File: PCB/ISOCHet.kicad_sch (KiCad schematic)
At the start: 19 parts, among them J1 USB_C_Receptacle_USB2.0, J2 Conn_01x08_Pin, SW0 BOOT, SW1 TAB, SW2 ENTER, SW3 CAPS, SW4 CAPS_STEP1.5, SW5 CAPS_STEP1.25, U1 CH552G, U2 USBLC6-2P6

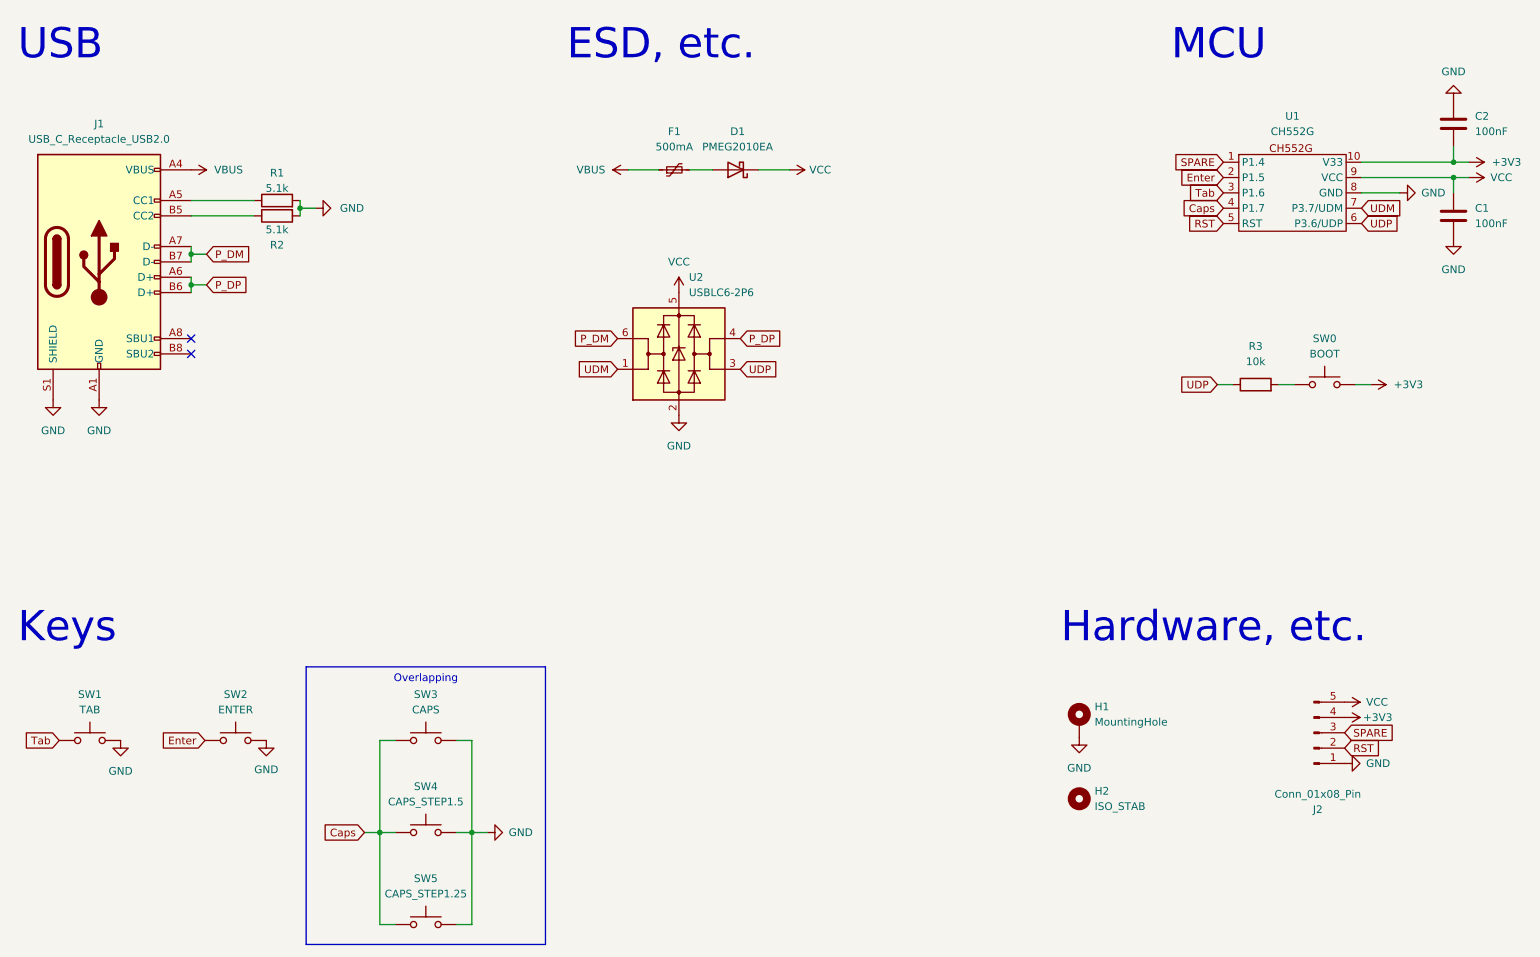
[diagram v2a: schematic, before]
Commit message: Move all components to front
USB data pins on port now line up with CH552E and do not need to crossover.
R1 and R2 remain on back.
Tweaked overlapping Caps Lock switch footprints to reduce DRC errors.
Power tracks are now 0.3mm to match maximum width of CH552E pads.
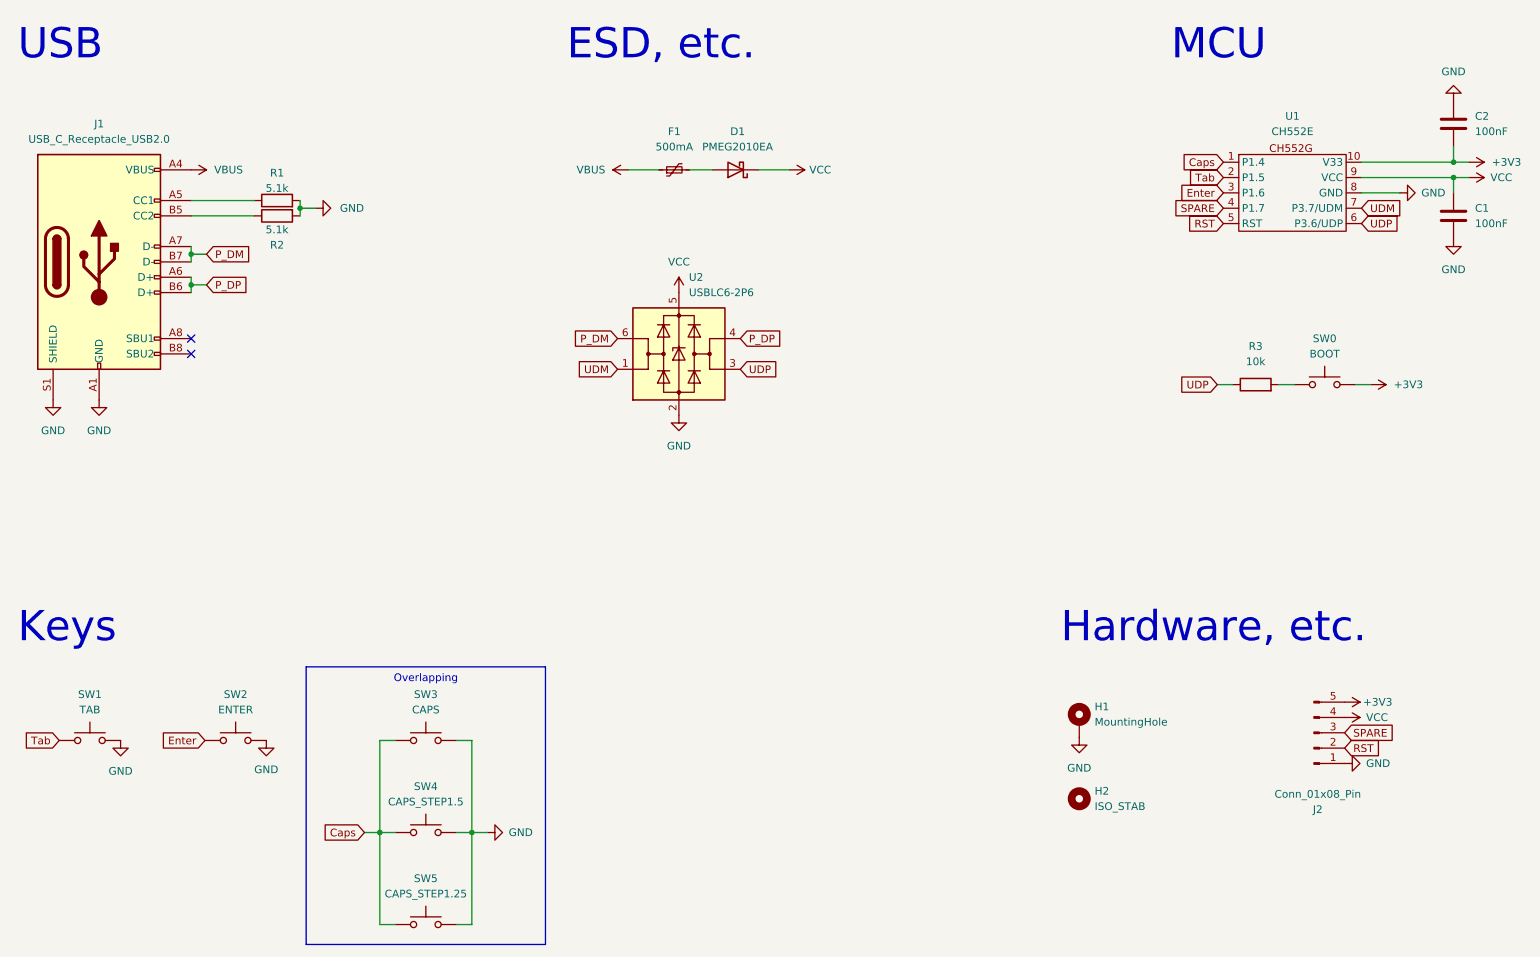
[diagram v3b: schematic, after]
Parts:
- U1: value CH552G -> CH552E; LCSC C111292 -> C967938
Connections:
- net +3V3: now also J2.5 (Pin_5); no longer J2.4 (Pin_4)
- net Caps: now also SW3.1, SW4.1, SW5.1, U1.1 (P1.4); no longer SW3.2, SW4.2, SW5.2, U1.4 (P1.7)
- net Enter: now also U1.3 (P1.6); no longer U1.2 (P1.5)
- net GND: now also SW1.2, SW3.2, SW4.2, SW5.2; no longer SW1.1, SW3.1, SW4.1, SW5.1
- net SPARE: now also U1.4 (P1.7); no longer U1.1 (P1.4)
- net Tab: now also SW1.1, U1.2 (P1.5); no longer SW1.2, U1.3 (P1.6)
- net VCC: now also J2.4 (Pin_4); no longer J2.5 (Pin_5)
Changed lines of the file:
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@@
     )
   )
-  (global_label "Caps" (shape input) (at 217.424 46.99 180) (fields_autoplaced)
+  (global_label "Caps" (shape input) (at 217.424 39.37 180) (fields_autoplaced)
     (effects (font (size 1.27 1.27)) (justify right))
-    (property "Intersheetrefs" "${INTERSHEET_REFS}" (at 209.8427 46.99 0)
+    (property "Intersheetrefs" "${INTERSHEET_REFS}" (at 209.8427 39.37 0)
       (effects (font (size 1.27 1.27)) (justify right) hide)
     )
@@
     )
   )
-  (global_label "Tab" (shape input) (at 217.424 44.45 180) (fields_autoplaced)
+  (global_label "Tab" (shape input) (at 217.424 41.91 180) (fields_autoplaced)
     (effects (font (size 1.27 1.27)) (justify right))
-    (property "Intersheetrefs" "${INTERSHEET_REFS}" (at 211.1732 44.45 0)
+    (property "Intersheetrefs" "${INTERSHEET_REFS}" (at 211.1732 41.91 0)
       (effects (font (size 1.27 1.27)) (justify right) hide)
     )
@@
     )
   )
-  (global_label "Enter" (shape input) (at 217.424 41.91 180) (fields_autoplaced)
+  (global_label "Enter" (shape input) (at 217.424 44.45 180) (fields_autoplaced)
     (effects (font (size 1.27 1.27)) (justify right))
-    (property "Intersheetrefs" "${INTERSHEET_REFS}" (at 209.5403 41.91 0)
+    (property "Intersheetrefs" "${INTERSHEET_REFS}" (at 209.5403 44.45 0)
       (effects (font (size 1.27 1.27)) (justify right) hide)
     )
   )
-  (global_label "SPARE" (shape input) (at 217.424 39.37 180) (fields_autoplaced)
+  (global_label "SPARE" (shape input) (at 217.424 46.99 180) (fields_autoplaced)
     (effects (font (size 1.27 1.27)) (justify right))
-    (property "Intersheetrefs" "${INTERSHEET_REFS}" (at 208.4517 39.37 0)
+    (property "Intersheetrefs" "${INTERSHEET_REFS}" (at 208.4517 46.99 0)
       (effects (font (size 1.27 1.27)) (justify right) hide)
     )
@@
     )
   )
-  (symbol (lib_id "power:+3V3") (at 237.49 131.318 270) (unit 1)
+  (symbol (lib_id "power:+3V3") (at 237.49 128.778 270) (unit 1)
     (in_bom yes) (on_board yes) (dnp no)
-    (property "Reference" "#PWR020" (at 233.68 131.318 0)
-      (effects (font (size 1.27 1.27)) hide)
-    )
-    (property "Value" "+3V3" (at 240.538 131.318 90)
-      (effects (font (size 1.27 1.27)) (justify left))
-    )
-    (property "Footprint" "" (at 237.49 131.318 0)
-      (effects (font (size 1.27 1.27)) hide)
-    )
-    (property "Datasheet" "" (at 237.49 131.318 0)
+    (property "Reference" "#PWR020" (at 233.68 128.778 0)
+      (effects (font (size 1.27 1.27)) hide)
+    )
+    (property "Value" "+3V3" (at 240.538 128.778 90)
+      (effects (font (size 1.27 1.27)) (justify left))
+    )
+    (property "Footprint" "" (at 237.49 128.778 0)
+      (effects (font (size 1.27 1.27)) hide)
+    )
+    (property "Datasheet" "" (at 237.49 128.778 0)
       (effects (font (size 1.27 1.27)) hide)
     )
@@
     )
   )
-  (symbol (lib_id "power:VCC") (at 237.49 128.778 270) (unit 1)
+  (symbol (lib_id "power:VCC") (at 237.49 131.318 270) (unit 1)
     (in_bom yes) (on_board yes) (dnp no)
-    (property "Reference" "#PWR022" (at 233.68 128.778 0)
-      (effects (font (size 1.27 1.27)) hide)
-    )
-    (property "Value" "VCC" (at 241.046 128.778 90)
-      (effects (font (size 1.27 1.27)) (justify left))
-    )
-    (property "Footprint" "" (at 237.49 128.778 0)
-      (effects (font (size 1.27 1.27)) hide)
-    )
-    (property "Datasheet" "" (at 237.49 128.778 0)
+    (property "Reference" "#PWR022" (at 233.68 131.318 0)
+      (effects (font (size 1.27 1.27)) hide)
+    )
+    (property "Value" "VCC" (at 241.046 131.318 90)
+      (effects (font (size 1.27 1.27)) (justify left))
+    )
+    (property "Footprint" "" (at 237.49 131.318 0)
+      (effects (font (size 1.27 1.27)) hide)
+    )
+    (property "Datasheet" "" (at 237.49 131.318 0)
       (effects (font (size 1.27 1.27)) hide)
     )
@@
     )
   )
-  (symbol (lib_id "Switch:SW_Push") (at 85.344 165.608 0) (mirror y) (unit 1)
+  (symbol (lib_id "Switch:SW_Push") (at 85.344 165.608 0) (unit 1)
     (in_bom no) (on_board yes) (dnp no)
     (property "Reference" "SW5" (at 85.344 157.988 0)
@@
     )
   )
-  (symbol (lib_id "Switch:SW_Push") (at 85.344 150.368 0) (mirror y) (unit 1)
+  (symbol (lib_id "Switch:SW_Push") (at 85.344 150.368 0) (unit 1)
     (in_bom no) (on_board yes) (dnp no)
     (property "Reference" "SW4" (at 85.344 142.748 0)
@@
     )
   )
-  (symbol (lib_id "Switch:SW_Push") (at 85.344 135.128 0) (mirror y) (unit 1)
+  (symbol (lib_id "Switch:SW_Push") (at 85.344 135.128 0) (unit 1)
     (in_bom yes) (on_board yes) (dnp no)
     (property "Reference" "SW3" (at 85.344 127.508 0)
@@
     )
   )
-  (symbol (lib_id "Switch:SW_Push") (at 29.718 135.128 0) (mirror y) (unit 1)
+  (symbol (lib_id "Switch:SW_Push") (at 29.718 135.128 0) (unit 1)
     (in_bom yes) (on_board yes) (dnp no)
     (property "Reference" "SW1" (at 29.718 127.508 0)
@@
       (effects (font (size 1.27 1.27)))
     )
-    (property "Value" "CH552G" (at 228.854 34.29 0)
+    (property "Value" "CH552E" (at 228.854 34.29 0)
       (effects (font (size 1.27 1.27)))
     )
@@
       (effects (font (size 1.27 1.27)) hide)
     )
-    (property "LCSC" "C111292" (at 228.6 48.26 0)
-      (effects (font (size 1.27 1.27)) hide)
-    )
+    (property "LCSC" "C967938" (at 228.6 48.26 0)
+      (effects (font (size 1.27 1.27)) hide)
+    )

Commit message: Switch USBLC6 (U2) to cheaper LCSC part number
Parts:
- U2: LCSC C2687116 -> C2827654
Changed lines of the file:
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@@
       (effects (font (size 1.27 1.27)) hide)
     )
-    (property "LCSC" "C2687116" (at 127.254 71.12 0)
+    (property "LCSC" "C2827654" (at 127.254 71.12 0)
       (effects (font (size 1.27 1.27)) hide)
     )

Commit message: Change R3 footprint to combined THT/SMD
I realised I had a bunch of DIN0207 axial 10kΩ resistors, so switched the footprint for R3 to support *either* through hole *or* surface mount. I looked at doing the same for R1 and R2, but fitting a THT resistor while keeping the USB port ground plane relatively isolated proved to be too troublesome.
Also fixed a DRC error on the VCC line into U1.
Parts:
- R3: footprint Resistor_SMD:R_0603_1608Metric_Pad0.98x0.95mm_HandSolder -> Project Library:R_Combined_DIN0207_1608
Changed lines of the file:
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@@
       (effects (font (size 1.27 1.27)))
     )
-    (property "Footprint" "Resistor_SMD:R_0603_1608Metric_Pad0.98x0.95mm_HandSolder" (at 222.758 77.978 90)
+    (property "Footprint" "Project Library:R_Combined_DIN0207_1608" (at 222.758 77.978 90)
       (effects (font (size 1.27 1.27)) hide)
     )

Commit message: Redo isolated ground
Removed keep-out zones between parts of GND plane. Instead, moved USB port to “Earth” net and added a “jumper” between Earth and GND. The jumper is a simple custom footprint with three pairs of overlapping pads that replaces the previous GND-to-GND traces. New Earth zones have been added on the front and back cooper layers.

R1 and R2 have been relocated to above and below the USB port’s pins rather than being left and right of the port. This simplifies their routing.
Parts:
- added JP1: Jumper_2_Bridged, Project Library:Ground_Isolation_Jumper, symbol Jumper:Jumper_2_Bridged
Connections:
- net GND: now also JP1.2 (B); no longer J1.A1 (GND), J1.A12 (GND), J1.B1 (GND), J1.B12 (GND), J1.S1 (SHIELD), R1.2, R2.2
- new net Earth: J1.A1 (GND), J1.A12 (GND), J1.B1 (GND), J1.B12 (GND), J1.S1 (SHIELD), JP1.1 (A), R1.2, R2.2
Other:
- moved on the sheet: U2

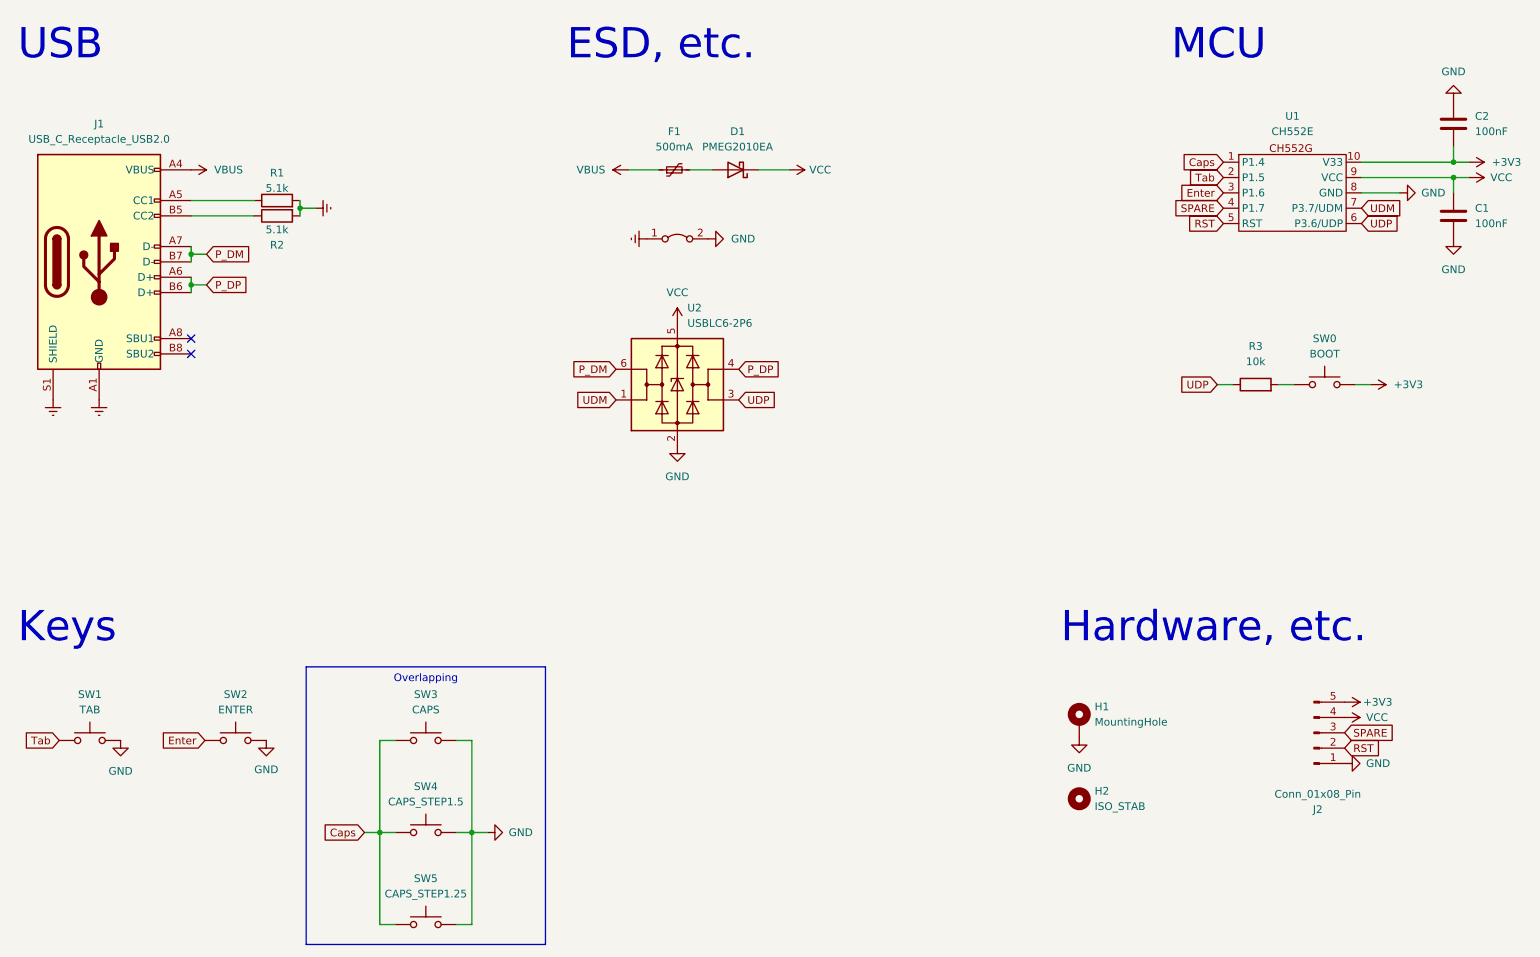
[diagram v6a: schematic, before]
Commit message: Connect USBLC6 to isolated ground
The USB ground (“Earth”) zone extends further down the board and the U2 ground pin connects to it and to H1 (the central mounting hole). H1 now has two pins and serves as the bridge between the two ground zones.

Also:

 * Switch U2 to more accurate USBLC6-2**SC6**
 * Remove all silkscreen from back except “R1” and “R2”
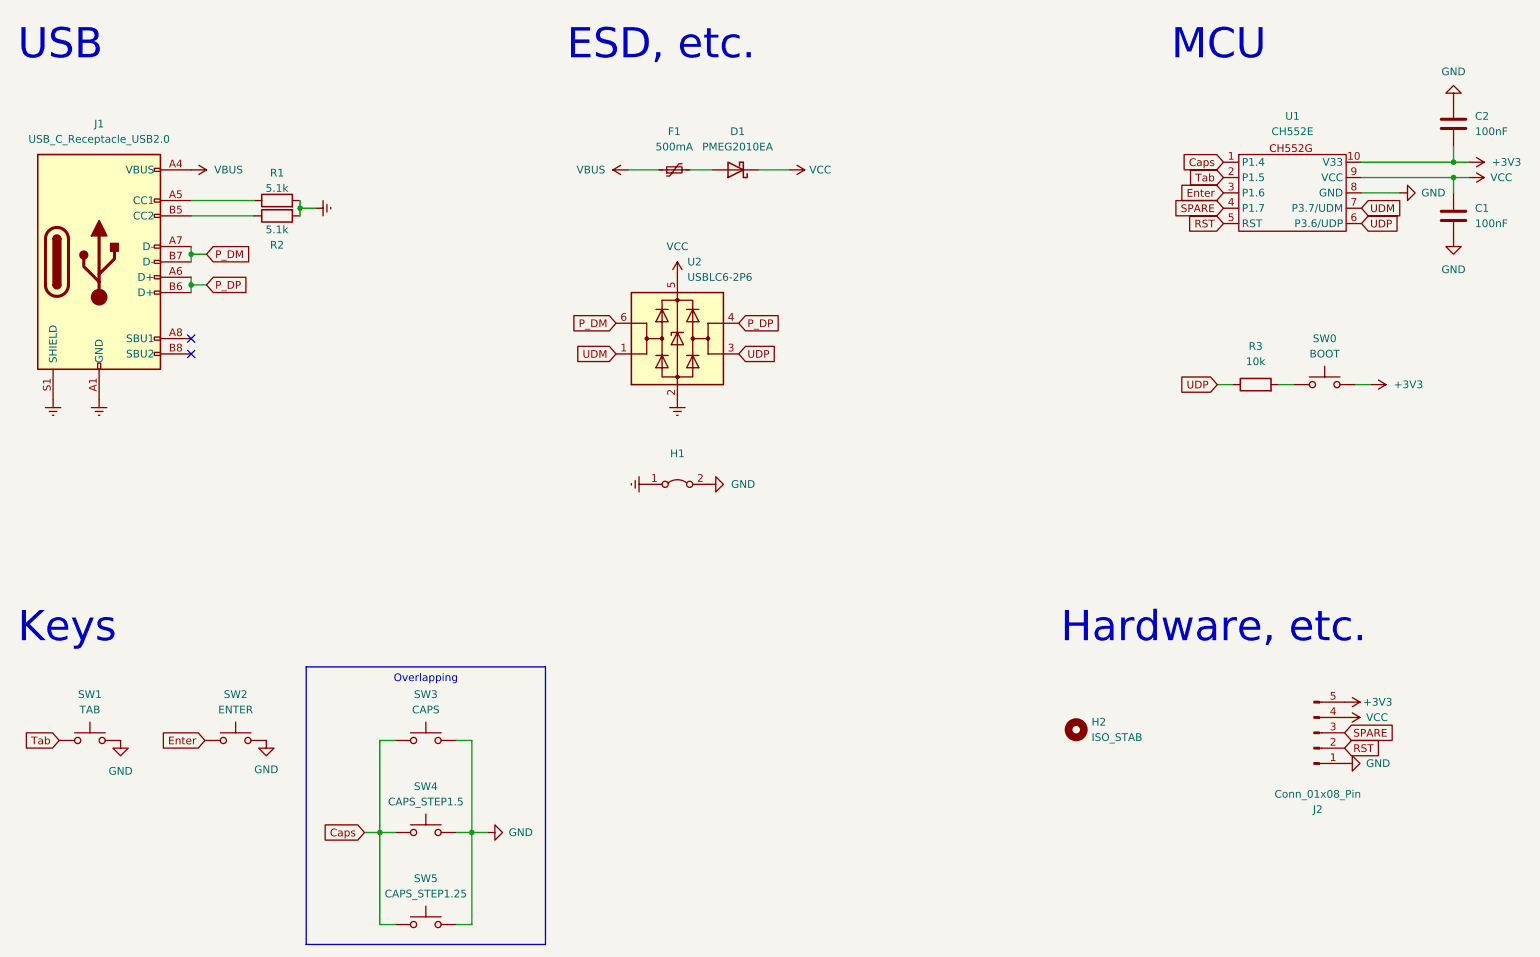
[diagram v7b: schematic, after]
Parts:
- removed H1: MountingHole, MountingHole:MountingHole_2.2mm_M2_DIN965_Pad, symbol Mechanical:MountingHole_Pad
- H1: renamed from JP1; value Jumper_2_Bridged -> Mounting Hole/Isolated Ground Jumper; footprint Project Library:Ground_Isolation_Jumper -> Project Library:MountingHole_2.2mm_M2_DIN965_Pad_Isolated_Ground_Jumper
- R1, R2: footprint Resistor_SMD:R_0603_1608Metric_Pad0.98x0.95mm_HandSolder -> Project Library:R_0603_1608Metric_Pad0.98x0.95mm_HandSolder
- U2: symbol Power_Protection:USBLC6-2P6 -> Power_Protection:USBLC6-2SC6
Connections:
- net Earth: now also U2.2 (GND)
- net GND: no longer U2.2 (GND)
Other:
- moved on the sheet: H2, U2
